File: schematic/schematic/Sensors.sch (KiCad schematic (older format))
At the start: 13 parts, among them J10 Conn_I2CBridge, J11 Conn_PBridge, J12 Conn__PBridge, J7 Conn_I2C, J8 Conn_SPI, J9 Conn__I2CBridge, U8 INA219AIDCNR

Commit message: やっぱり機能を絞るに限る
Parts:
- removed J10: Conn_I2CBridge, Connector_PinHeader_1.00mm:PinHeader_2x03_P1.00mm_Vertical_SMD, symbol Connector_Generic:Conn_01x02
- removed J12: Conn__PBridge, Connector_PinHeader_1.00mm:PinHeader_2x03_P1.00mm_Vertical_SMD, symbol Connector_Generic:Conn_01x05
- removed J9: Conn__I2CBridge, Connector_PinHeader_1.00mm:PinHeader_2x03_P1.00mm_Vertical_SMD, symbol Connector_Generic:Conn_01x02
- removed R34, R35: 10, micelib:C_0402_1005Metric_HandSoldering, symbol Device:R_Small
- added C21: 0.1u, micelib:C_0402_1005Metric_HandSoldering, symbol Device:C_Small
- added J10, J12, J9: Conn_01x06, Connector_PinHeader_1.00mm:PinHeader_2x03_P1.00mm_Vertical_SMD, symbol Connector_Generic:Conn_01x06
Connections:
- net +3V3: now also C21.1, J12.3 (Pin_3)
- net +5V: now also C19.1, U8.1 (IN+), J12.4 (Pin_4)
- net ADC1_Batt: now also J10.4 (Pin_4), J9.4 (Pin_4); no longer J11.5 (Pin_5)
- net GNDD: now also J11.5 (Pin_5), C21.2, J10.3 (Pin_3), J10.5 (Pin_5), J10.6 (Pin_6), J12.1 (Pin_1), J12.2 (Pin_2), J12.5 (Pin_5), J9.1 (Pin_1), J9.2 (Pin_2), J9.3 (Pin_3)
- net I2C_SCL: now also J7.2 (Pin_2), J10.1 (Pin_1), J9.5 (Pin_5); no longer J7.1 (Pin_1)
- net I2C_SDA: now also J7.1 (Pin_1), J10.2 (Pin_2), J9.6 (Pin_6); no longer J7.2 (Pin_2)
- net MD_VM: now also C19.2, U8.2 (IN-)
- net SPI_CLK: now also J8.3 (Pin_3); no longer J8.1 (Pin_1)
- net SPI_MISO: now also J8.1 (Pin_1); no longer J8.3 (Pin_3)
- net VBUS: now also J12.6 (Pin_6)
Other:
- moved on the sheet: C19, R33, U8

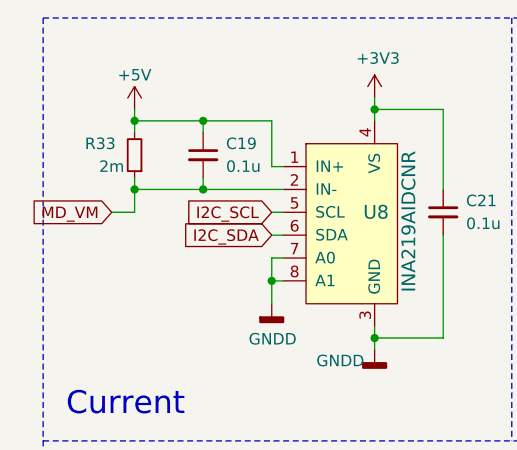
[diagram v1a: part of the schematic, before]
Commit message: サーボとIMUが動いた
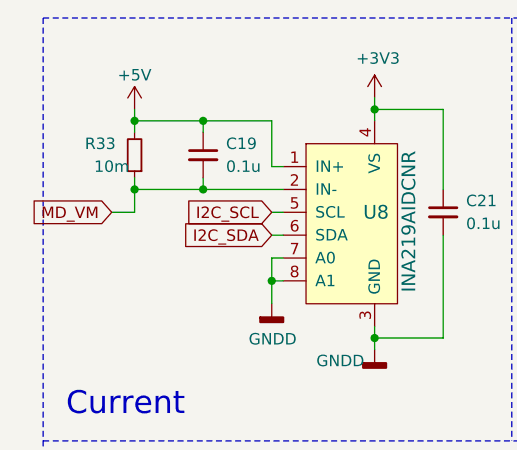
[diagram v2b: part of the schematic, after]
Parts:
- R33: value 2m -> 10m
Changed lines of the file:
@@
 AR Path="/5E247314/5E291C2D" Ref="R33"  Part="1"
 F 0 "R33" H 1150 1150 50  0000 C CNN
-F 1 "2m" H 1100 1250 50  0000 C CNN
+F 1 "10m" H 1100 1250 50  0000 C CNN
 F 2 "micelib:C_0402_1005Metric_HandSoldering" H 1000 1200 50  0001 C CNN
 F 3 "~" H 1000 1200 50  0001 C CNN
